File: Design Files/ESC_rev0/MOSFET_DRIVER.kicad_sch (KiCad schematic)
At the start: 0 parts

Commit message: update3
Added DRV8302 footprint and started the Mosfet driver schematic.
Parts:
- added R11: 205k, symbol Device:R
- added U2: DRV8302DCA, DCA56_6P35X3P61, symbol DRV8302:DRV8302DCA
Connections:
- new net: R11.2, U2.1 (RT_CLK)
- new net GND: R11.1
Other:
- note added: "${TITLE}"
- note added: "Mount this resistor close as possible to RT_CLK pin"
- title: (none) -> Mosfet Driver

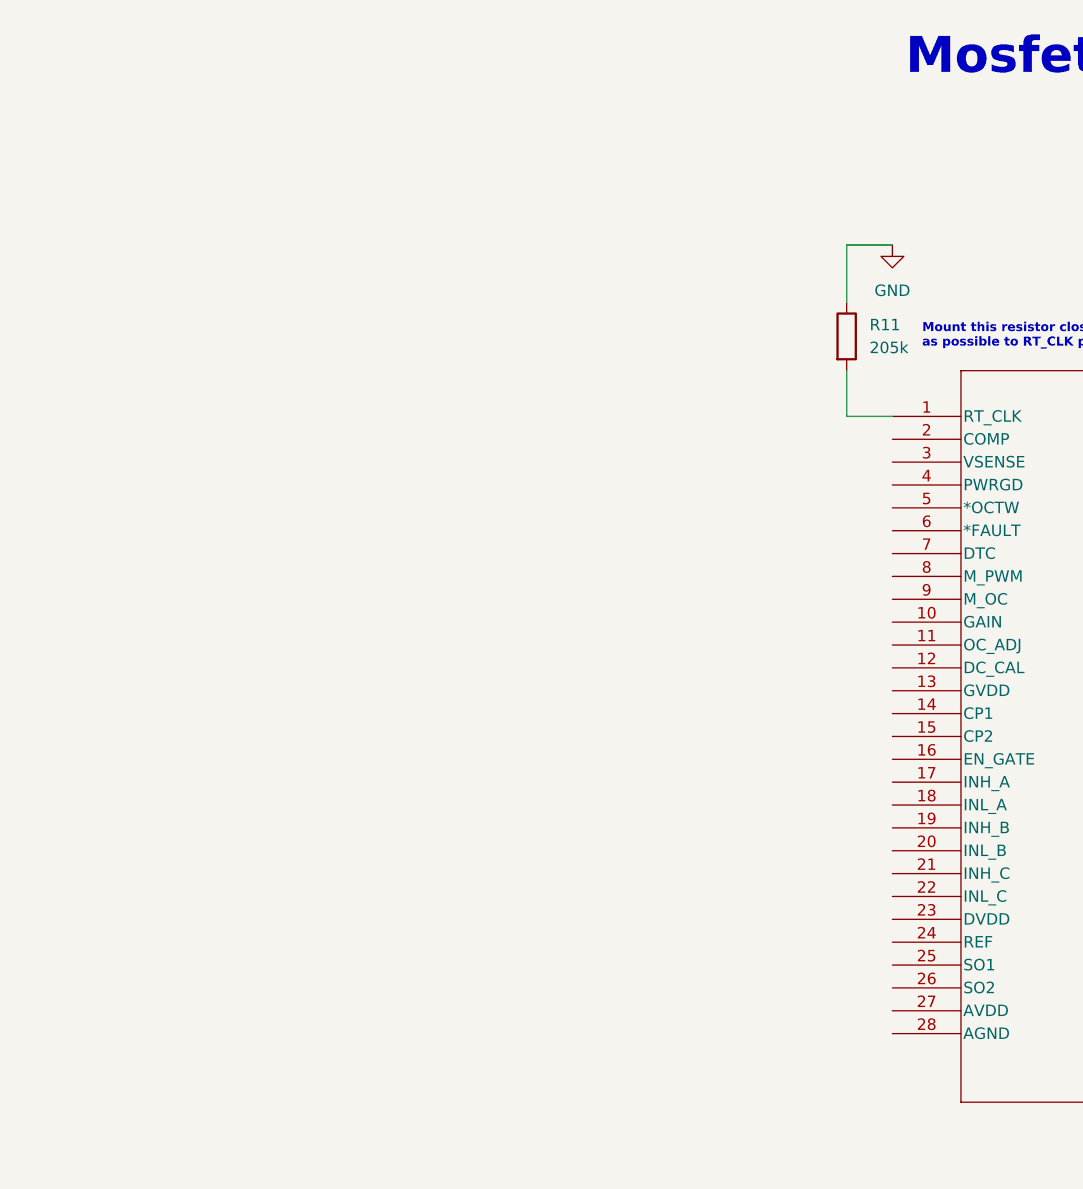
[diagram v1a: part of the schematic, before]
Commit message: update4
gate driver left side complete
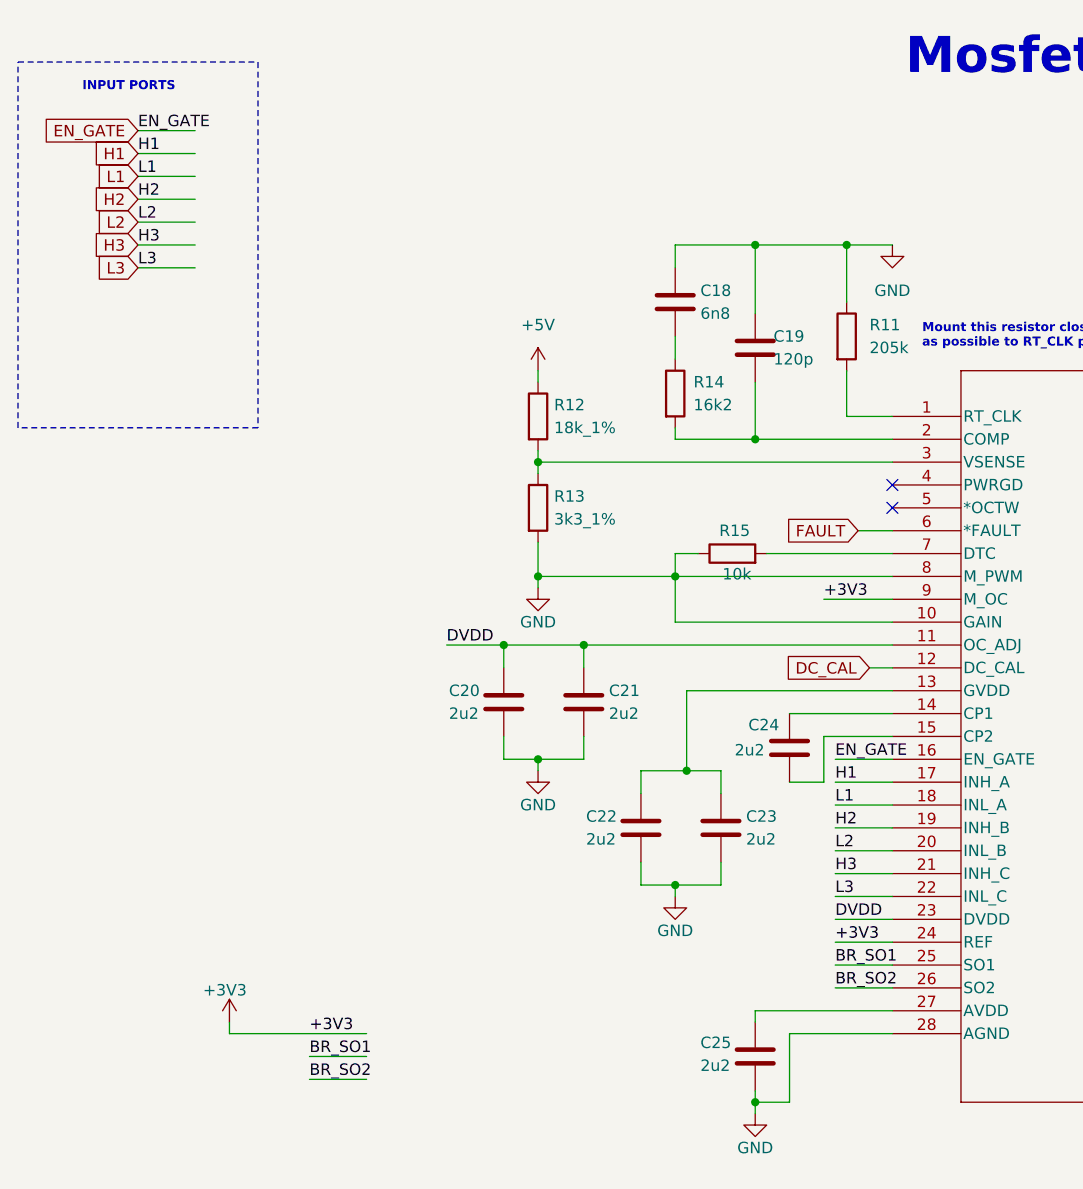
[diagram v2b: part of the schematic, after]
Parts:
- added C18: 6n8, symbol Device:C
- added C19: 120p, symbol Device:C
- added C20, C21, C22, C23, C24, C25: 2u2, symbol Device:C
- added R12: 18k_1%, symbol Device:R
- added R13: 3k3_1%, symbol Device:R
- added R14: 16k2, symbol Device:R
- added R15: 10k, symbol Device:R
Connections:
- net GND: now also U2.10 (GAIN), U2.28 (AGND), U2.8 (M_PWM), C18.1, C19.1, C20.2, C21.2, C22.2, C23.2, C25.2, R13.2, R15.1
- net DVDD: now reaches U2.11 (OC_ADJ)
- net DVDD: now also U2.23 (DVDD), C20.1, C21.1
- net DC_CAL: now reaches U2.12 (DC_CAL)
- net at U2.13 (GVDD): now also C22.1, C23.1
- net at U2.14 (CP1): now also C24.1
- net at U2.15 (CP2): now also C24.2
- net EN_GATE: now reaches U2.16 (EN_GATE)
- net H1: now reaches U2.17 (INH_A)
- net L1: now reaches U2.18 (INL_A)
- net H2: now reaches U2.19 (INH_B)
- net at U2.2 (COMP): now also C19.2, R14.2
- net L2: now reaches U2.20 (INL_B)
- net H3: now reaches U2.21 (INH_C)
- net L3: now reaches U2.22 (INL_C)
- net +3V3: now reaches U2.24 (REF)
- net +3V3: now also U2.9 (M_OC)
- net BR_SO1: now reaches U2.25 (SO1)
- net BR_SO2: now reaches U2.26 (SO2)
- net at U2.27 (AVDD): now also C25.1
- net at U2.3 (VSENSE): now also R12.2, R13.1
- net FAULT: now reaches U2.6 (*FAULT)
- net at U2.7 (DTC): now also R15.2
- new net: C18.2, R14.1
- new net +5V: R12.1
- no-connect marks 0 -> 2
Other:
- note added: "INPUT PORTS"

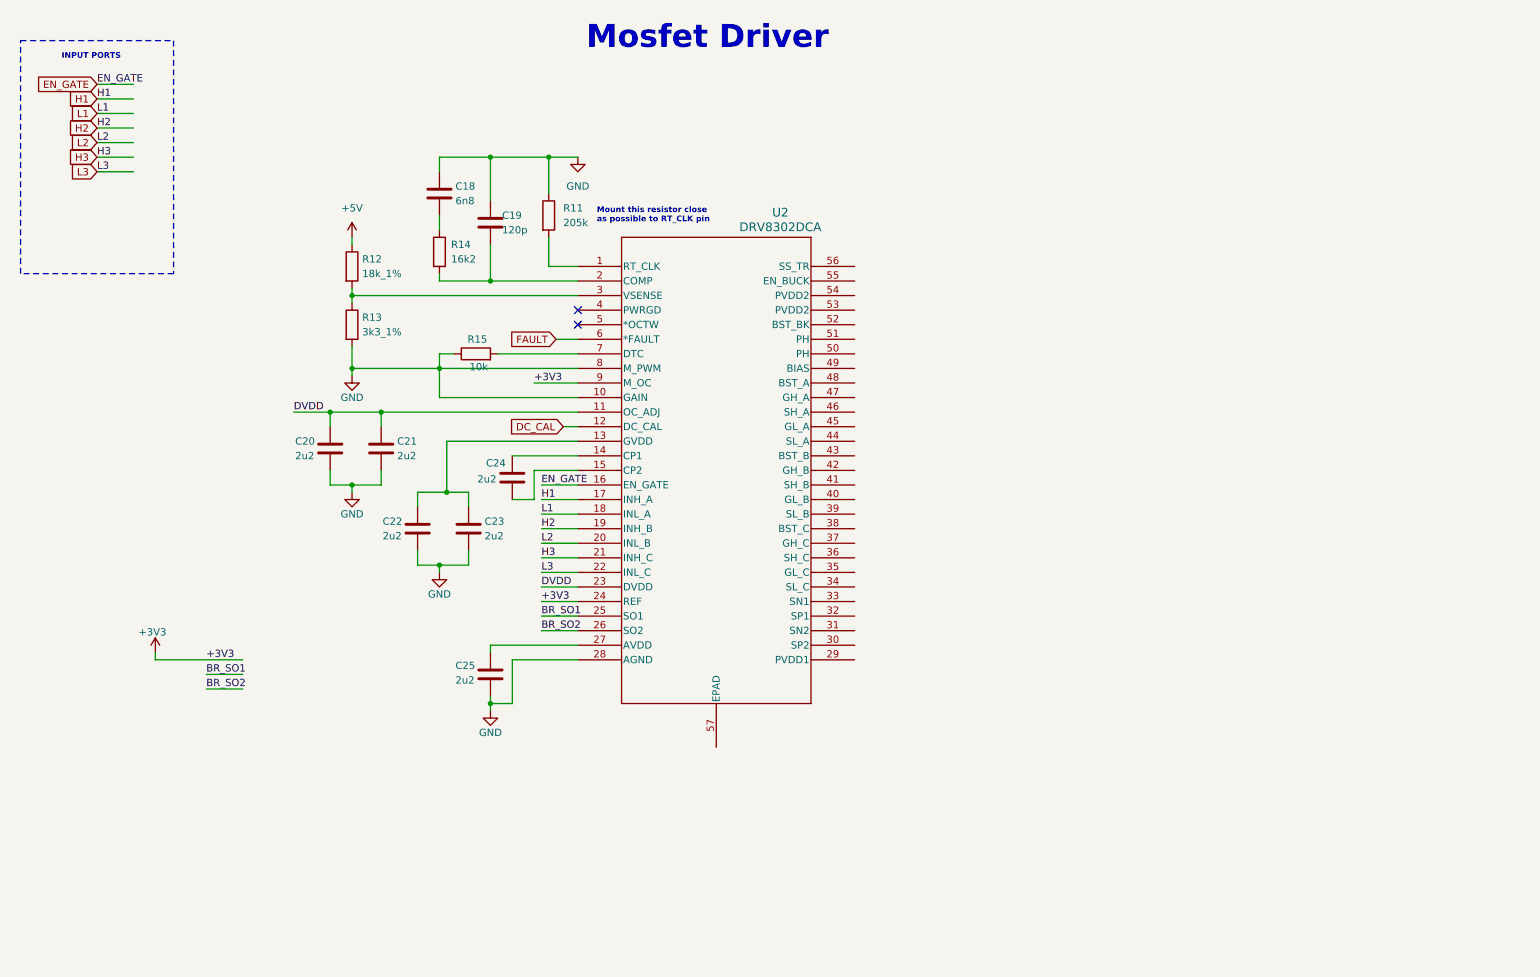
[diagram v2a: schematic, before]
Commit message: update 5
gate driver right side
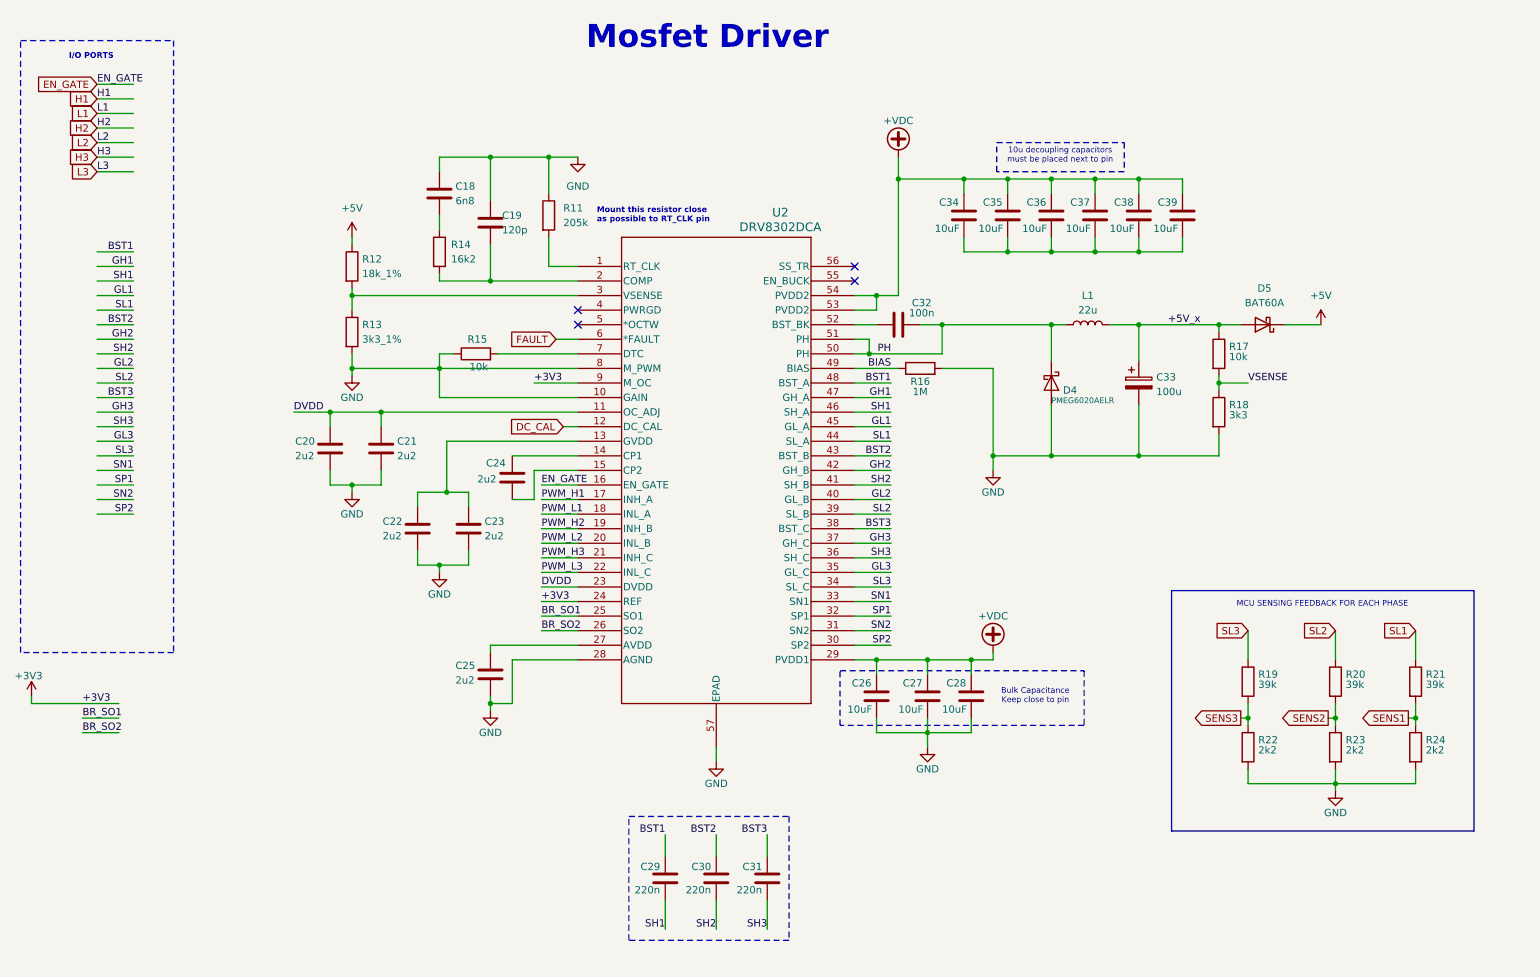
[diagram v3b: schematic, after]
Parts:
- added C26, C27, C28, C34, C35, C36, C37, C38, C39: 10uF, symbol Device:C
- added C29, C30, C31: 220n, symbol Device:C
- added C32: 100n, symbol Device:C
- added C33: 100u, symbol Device:C_Polarized
- added D4: PMEG6020AELR, Diode_SMD:Nexperia_CFP3_SOD-123W, symbol Diode:PMEG6020AELR
- added D5: BAT60A, Diode_SMD:D_SOD-323, symbol Diode:BAT60A
- added L1: 22u, symbol Device:L
- added R16: 1M, symbol Device:R
- added R17: 10k, symbol Device:R
- added R18: 3k3, symbol Device:R
- added R19, R20, R21: 39k, symbol Device:R
- added R22, R23, R24: 2k2, symbol Device:R
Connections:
- net +5V: now also D5.1 (K)
- net GND: now also U2.57 (EPAD), C26.2, C27.2, C28.2, C33.2, D4.2 (A), R16.2, R18.2, R22.2, R23.2, R24.2
- net H1: no longer U2.17 (INH_A)
- net H2: no longer U2.19 (INH_B)
- net H3: no longer U2.21 (INH_C)
- net L1: no longer U2.18 (INL_A)
- net L2: no longer U2.20 (INL_B)
- net L3: no longer U2.22 (INL_C)
- net +VDC: now reaches U2.29 (PVDD1)
- net +VDC: now also U2.53 (PVDD2), U2.54 (PVDD2), C26.1, C27.1, C28.1, C34.1, C35.1, C36.1, C37.1, C38.1, C39.1
- net SP2: now reaches U2.30 (SP2)
- net SN2: now reaches U2.31 (SN2)
- net SP1: now reaches U2.32 (SP1)
- net SN1: now reaches U2.33 (SN1)
- net SL3: now reaches U2.34 (SL_C)
- net SL3: now also R19.1
- net GL3: now reaches U2.35 (GL_C)
- net SH3: now reaches U2.36 (SH_C)
- net SH3: now also C31.2
- net GH3: now reaches U2.37 (GH_C)
- net BST3: now reaches U2.38 (BST_C)
- net BST3: now also C31.1
- net SL2: now reaches U2.39 (SL_B)
- net SL2: now also R20.1
- net GL2: now reaches U2.40 (GL_B)
- net SH2: now reaches U2.41 (SH_B)
- net SH2: now also C30.2
- net GH2: now reaches U2.42 (GH_B)
- net BST2: now reaches U2.43 (BST_B)
- net BST2: now also C30.1
- net SL1: now reaches U2.44 (SL_A)
- net SL1: now also R21.1
- net GL1: now reaches U2.45 (GL_A)
- net SH1: now reaches U2.46 (SH_A)
- net SH1: now also C29.2
- net GH1: now reaches U2.47 (GH_A)
- net BST1: now reaches U2.48 (BST_A)
- net BST1: now also C29.1
- net BIAS: now reaches U2.49 (BIAS)
- net BIAS: now also R16.1
- net PH: now reaches U2.50 (PH)
- net PH: now also U2.51 (PH), C32.2, D4.1 (K), L1.1
- net at U2.52 (BST_BK): now also C32.1
- new net: C34.2, C35.2, C36.2, C37.2, C38.2, C39.2
- new net +5V_x: C33.1, D5.2 (A), L1.2, R17.1
- new net PWM_H1: U2.17 (INH_A)
- new net PWM_H2: U2.19 (INH_B)
- new net PWM_H3: U2.21 (INH_C)
- new net PWM_L1: U2.18 (INL_A)
- new net PWM_L2: U2.20 (INL_B)
- new net PWM_L3: U2.22 (INL_C)
- new net SENS1: R21.2, R24.1
- new net SENS2: R20.2, R23.1
- new net SENS3: R19.2, R22.1
- new net VSENSE: R17.2, R18.1
- no-connect marks 2 -> 4
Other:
- note added: "10u decoupling capacitors must be placed next to pin"
- note added: "Bulk Capacitance Keep close to pin"
- note added: "I/O PORTS"
- note added: "MCU SENSING FEEDBACK FOR EACH PHASE"
- note removed: "INPUT PORTS"
- moved on the sheet: R13

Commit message: update 6
gate driver completion and mosfet init
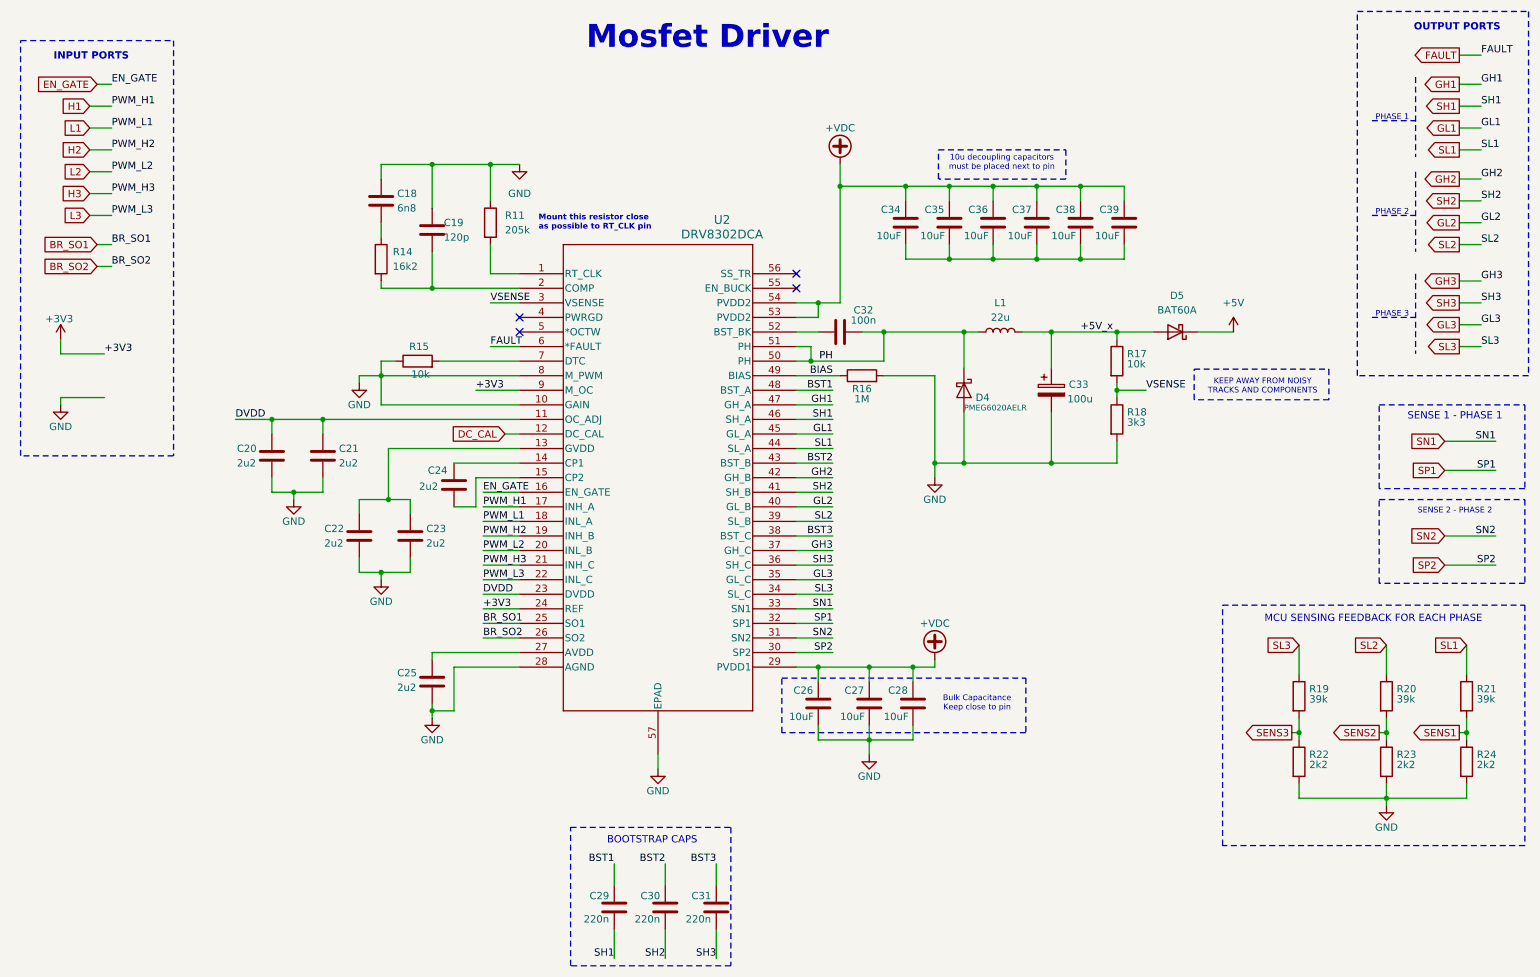
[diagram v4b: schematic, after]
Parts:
- removed R12: 18k_1%, symbol Device:R
- removed R13: 3k3_1%, symbol Device:R
- L1: footprint (none) -> PowerInductorSMD:IND-SMD_L7.8-W7.8_SDR0805
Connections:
- net PWM_H1 is gone; now on net H1: U2.17 (INH_A)
- net PWM_H2 is gone; now on net H2: U2.19 (INH_B)
- net PWM_H3 is gone; now on net H3: U2.21 (INH_C)
- net PWM_L1 is gone; now on net L1: U2.18 (INL_A)
- net PWM_L2 is gone; now on net L2: U2.20 (INL_B)
- net PWM_L3 is gone; now on net L3: U2.22 (INL_C)
- net VSENSE: now also U2.3 (VSENSE)
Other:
- note added: "BOOTSTRAP CAPS"
- note added: "INPUT PORTS"
- note added: "KEEP AWAY FROM NOISY TRACKS AND COMPONENTS"
- note added: "OUTPUT PORTS"
- note added: "PHASE 1"
- note added: "PHASE 2"
- note added: "PHASE 3"
- note added: "SENSE 1 - PHASE 1"
- note added: "SENSE 2 - PHASE 2"
- note removed: "I/O PORTS"
- moved on the sheet: C18, C19, C20, C21, C22, C23, C24, C25, C26, C27, C28, C29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

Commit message: update 9
filters and USB complete
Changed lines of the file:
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@@
 					(italic yes)
 				)
-				(hide yes)
 			)
 		)
